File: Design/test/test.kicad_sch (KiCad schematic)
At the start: 5 parts

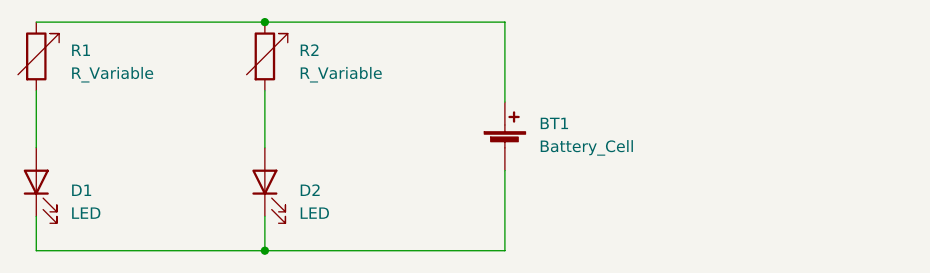
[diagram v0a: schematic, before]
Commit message: Added second battery
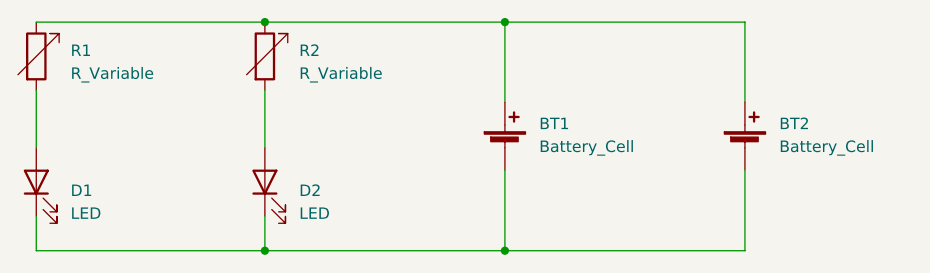
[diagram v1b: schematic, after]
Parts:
- added BT2: Battery_Cell, symbol Device:Battery_Cell
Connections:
- net at BT1.2 (-), D1.1 (K), D2.1 (K): now also BT2.2 (-)
- net at BT1.1 (+), R1.1, R2.1: now also BT2.1 (+)
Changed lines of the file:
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@@
 (kicad_sch (version 20230121) (generator eeschema)
   (paper "A4")
+  (junction (at 143.51 88.9) (diameter 0) (color 0 0 0 0)
+  )
   (junction (at 116.84 63.5) (diameter 0) (color 0 0 0 0)
   )
   (junction (at 116.84 88.9) (diameter 0) (color 0 0 0 0)
   )
+  (junction (at 143.51 63.5) (diameter 0) (color 0 0 0 0)
+  )
   (wire (pts (xy 143.51 72.39) (xy 143.51 63.5))
+    (stroke (width 0) (type default))
+  )
+  (wire (pts (xy 170.18 72.39) (xy 170.18 63.5))
+    (stroke (width 0) (type default))
+  )
+  (wire (pts (xy 170.18 80.01) (xy 170.18 88.9))
+    (stroke (width 0) (type default))
+  )
+  (wire (pts (xy 170.18 63.5) (xy 143.51 63.5))
     (stroke (width 0) (type default))
   )
@@
   )
   (wire (pts (xy 91.44 71.12) (xy 91.44 77.47))
+    (stroke (width 0) (type default))
+  )
+  (wire (pts (xy 170.18 88.9) (xy 143.51 88.9))
     (stroke (width 0) (type default))
   )
@@
     (stroke (width 0) (type default))
   )
+  (symbol (lib_id "Device:Battery_Cell") (at 170.18 77.47 0) (unit 1)
+    (in_bom yes) (on_board yes) (dnp no) (fields_autoplaced)
+    (property "Reference" "BT2" (at 173.99 74.803 0)
+      (effects (font (size 1.27 1.27)) (justify left))
+    )
+    (property "Value" "Battery_Cell" (at 173.99 77.343 0)
+      (effects (font (size 1.27 1.27)) (justify left))
+    )
+    (property "Footprint" "" (at 170.18 75.946 90)
+      (effects (font (size 1.27 1.27)) hide)
+    )
+    (property "Datasheet" "~" (at 170.18 75.946 90)
+      (effects (font (size 1.27 1.27)) hide)
+    )
+    (pin "1")
+    (pin "2")
+    (instances
+      (project "test"
+        (path "/52891afa-c894-4a65-b597-11a9623d8fcf"
+          (reference "BT2") (unit 1)
+        )
+      )
+    )
+  )
   (symbol (lib_id "Device:LED") (at 116.84 81.28 90) (unit 1)
